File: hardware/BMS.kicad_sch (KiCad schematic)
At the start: 21 parts, among them U3 BQ25887

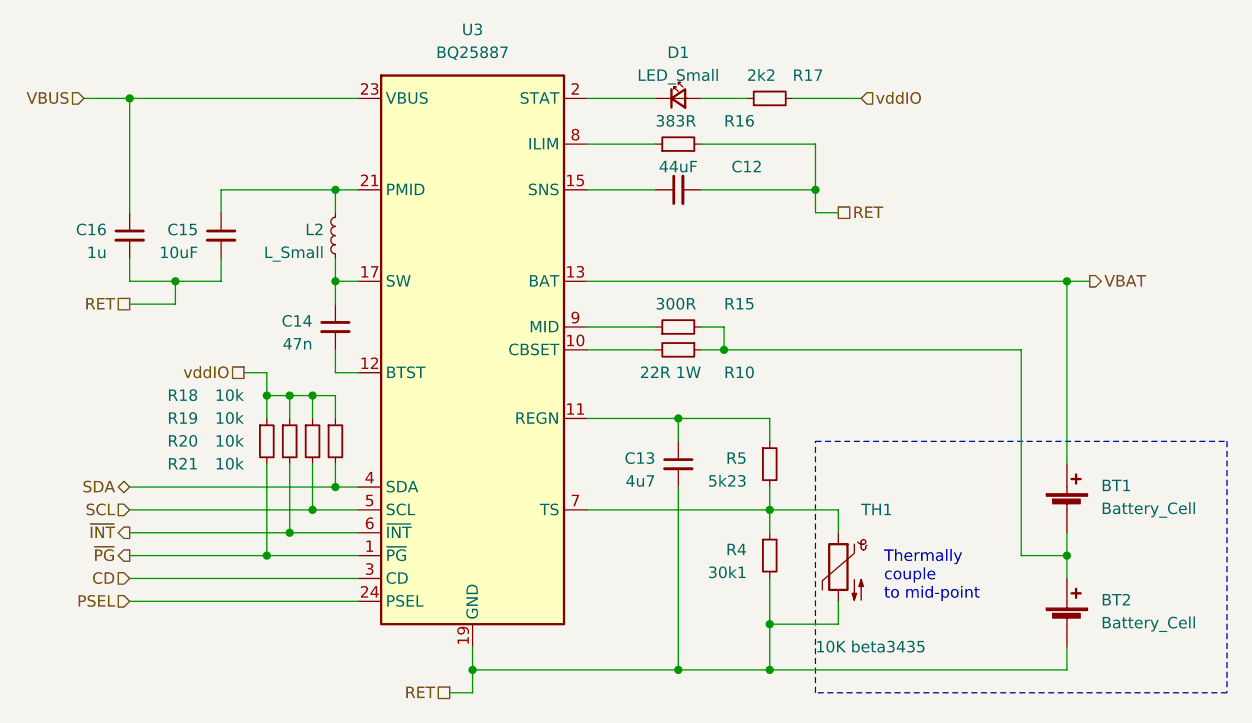
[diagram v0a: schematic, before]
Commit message: Some routing and pinout changes
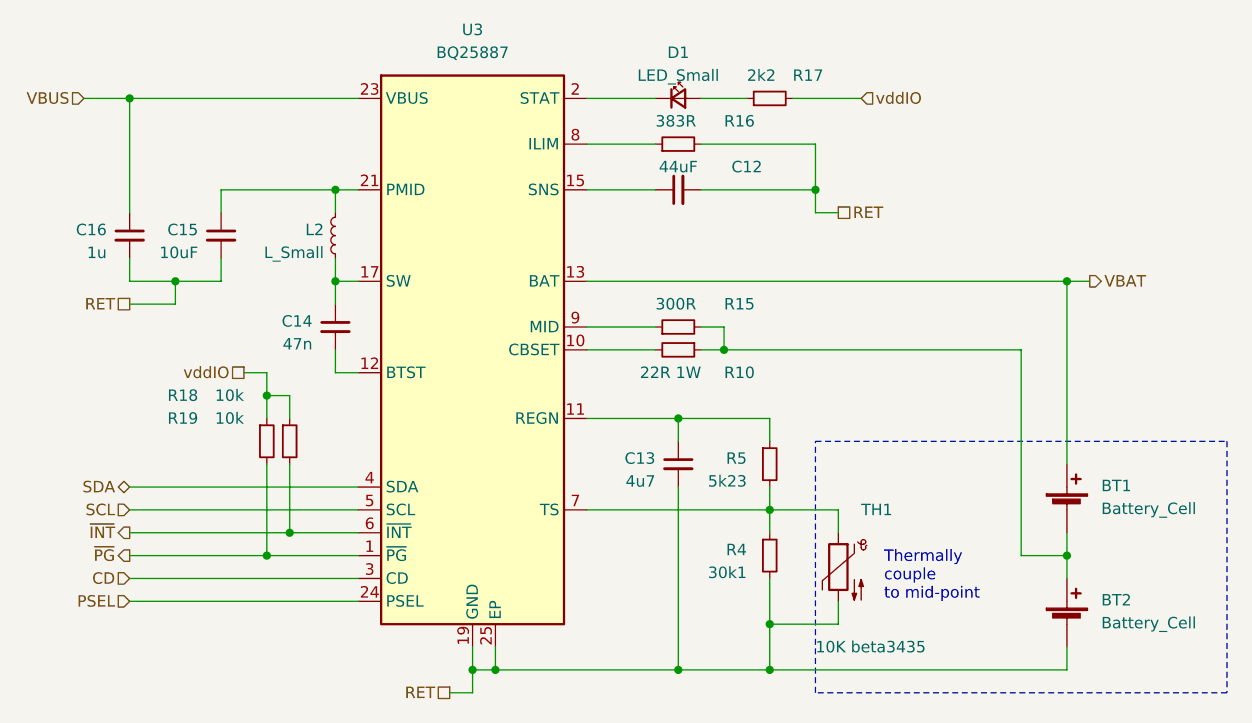
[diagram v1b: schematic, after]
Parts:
- removed R20, R21: 10k, symbol Device:R_Small
- C12: footprint (none) -> Capacitor_SMD:C_1210_3225Metric
- C13: footprint (none) -> Capacitor_SMD:C_0603_1608Metric
- C14, C16: footprint (none) -> Capacitor_SMD:C_0402_1005Metric
- C15: footprint (none) -> Capacitor_SMD:C_0805_2012Metric
- D1: footprint (none) -> LED_SMD:LED_0603_1608Metric
- R10: footprint (none) -> Resistor_SMD:R_1210_3225Metric
- R15: footprint (none) -> Resistor_SMD:R_0603_1608Metric
- R16, R17, R18, R19, R4, R5, TH1: footprint (none) -> Resistor_SMD:R_0402_1005Metric
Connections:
- net RET: now also U3.25 (EP)
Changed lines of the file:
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@@
 (kicad_sch (version 20230121) (generator eeschema)
   (paper "A4")
-  (junction (at 101.6 83.82) (diameter 0) (color 0 0 0 0)
-  )
   (junction (at 96.52 83.82) (diameter 0) (color 0 0 0 0)
   )
@@
   (junction (at 152.4 114.3) (diameter 0) (color 0 0 0 0)
   )
-  (junction (at 101.6 96.52) (diameter 0) (color 0 0 0 0)
-  )
   (junction (at 142.24 86.36) (diameter 0) (color 0 0 0 0)
   )
@@
   (junction (at 147.32 78.74) (diameter 0) (color 0 0 0 0)
   )
-  (junction (at 99.06 83.82) (diameter 0) (color 0 0 0 0)
-  )
   (junction (at 185.42 101.6) (diameter 0) (color 0 0 0 0)
   )
   (junction (at 152.4 96.52) (diameter 0) (color 0 0 0 0)
   )
+  (junction (at 121.92 114.3) (diameter 0) (color 0 0 0 0)
+  )
   (junction (at 104.14 60.96) (diameter 0) (color 0 0 0 0)
   )
@@
   (junction (at 152.4 109.22) (diameter 0) (color 0 0 0 0)
   )
-  (junction (at 104.14 93.98) (diameter 0) (color 0 0 0 0)
-  )
   (junction (at 81.28 50.8) (diameter 0) (color 0 0 0 0)
   )
@@
     (stroke (width 0) (type default))
   )
-  (wire (pts (xy 101.6 91.44) (xy 101.6 96.52))
-    (stroke (width 0) (type default))
-  )
   (wire (pts (xy 154.94 50.8) (xy 162.56 50.8))
     (stroke (width 0) (type default))
   )
-  (wire (pts (xy 119.38 114.3) (xy 142.24 114.3))
+  (wire (pts (xy 119.38 114.3) (xy 121.92 114.3))
     (stroke (width 0) (type default))
   )
@@
     (stroke (width 0) (type default))
   )
-  (wire (pts (xy 101.6 83.82) (xy 104.14 83.82))
-    (stroke (width 0) (type default))
-  )
   (wire (pts (xy 152.4 93.98) (xy 152.4 96.52))
     (stroke (width 0) (type default))
@@
     (stroke (width 0) (type default))
   )
-  (wire (pts (xy 101.6 83.82) (xy 101.6 86.36))
-    (stroke (width 0) (type default))
-  )
-  (wire (pts (xy 99.06 83.82) (xy 101.6 83.82))
-    (stroke (width 0) (type default))
-  )
-  (wire (pts (xy 81.28 93.98) (xy 104.14 93.98))
+  (wire (pts (xy 81.28 93.98) (xy 106.68 93.98))
     (stroke (width 0) (type default))
   )
@@
     (stroke (width 0) (type default))
   )
-  (wire (pts (xy 104.14 83.82) (xy 104.14 86.36))
-    (stroke (width 0) (type default))
-  )
   (wire (pts (xy 132.08 86.36) (xy 142.24 86.36))
     (stroke (width 0) (type default))
@@
     (stroke (width 0) (type default))
   )
-  (wire (pts (xy 104.14 91.44) (xy 104.14 93.98))
-    (stroke (width 0) (type default))
-  )
   (wire (pts (xy 104.14 63.5) (xy 104.14 60.96))
     (stroke (width 0) (type default))
@@
     (stroke (width 0) (type default))
   )
-  (wire (pts (xy 104.14 93.98) (xy 106.68 93.98))
-    (stroke (width 0) (type default))
-  )
   (wire (pts (xy 76.2 50.8) (xy 81.28 50.8))
     (stroke (width 0) (type default))
@@
     (stroke (width 0) (type default))
   )
+  (wire (pts (xy 121.92 111.76) (xy 121.92 114.3))
+    (stroke (width 0) (type default))
+  )
   (wire (pts (xy 93.98 81.28) (xy 96.52 81.28))
     (stroke (width 0) (type default))
@@
     (stroke (width 0) (type default))
   )
-  (wire (pts (xy 81.28 96.52) (xy 101.6 96.52))
-    (stroke (width 0) (type default))
-  )
   (wire (pts (xy 81.28 50.8) (xy 106.68 50.8))
     (stroke (width 0) (type default))
@@
     (stroke (width 0) (type default))
   )
-  (wire (pts (xy 101.6 96.52) (xy 106.68 96.52))
+  (wire (pts (xy 121.92 114.3) (xy 142.24 114.3))
+    (stroke (width 0) (type default))
+  )
+  (wire (pts (xy 81.28 96.52) (xy 106.68 96.52))
     (stroke (width 0) (type default))
   )
@@
       (effects (font (size 1.27 1.27)) (justify right))
     )
-    (property "Footprint" "" (at 96.52 88.9 0)
+    (property "Footprint" "Resistor_SMD:R_0402_1005Metric" (at 96.52 88.9 0)
       (effects (font (size 1.27 1.27)) hide)
     )
@@
       (effects (font (size 1.27 1.27)) (justify right))
     )
-    (property "Footprint" "" (at 152.4 50.8 0)
+    (property "Footprint" "Resistor_SMD:R_0402_1005Metric" (at 152.4 50.8 0)
       (effects (font (size 1.27 1.27)) hide)
     )
@@
       (effects (font (size 1.27 1.27)) (justify right))
     )
-    (property "Footprint" "" (at 142.24 91.44 0)
+    (property "Footprint" "Capacitor_SMD:C_0603_1608Metric" (at 142.24 91.44 0)
       (effects (font (size 1.27 1.27)) hide)
     )
@@
       (effects (font (size 1.27 1.27)) (justify right))
     )
-    (property "Footprint" "" (at 104.14 76.2 0)
+    (property "Footprint" "Capacitor_SMD:C_0402_1005Metric" (at 104.14 76.2 0)
       (effects (font (size 1.27 1.27)) hide)
     )
@@
       (effects (font (size 1.27 1.27)))
     )
-    (property "Footprint" "" (at 142.24 60.96 0)
+    (property "Footprint" "Capacitor_SMD:C_1210_3225Metric" (at 142.24 60.96 0)
       (effects (font (size 1.27 1.27)) hide)
     )
@@
       (effects (font (size 1.27 1.27)) (justify right))
     )
-    (property "Footprint" "" (at 160.02 101.6 0)
+    (property "Footprint" "Resistor_SMD:R_0402_1005Metric" (at 160.02 101.6 0)
       (effects (font (size 1.27 1.27)) hide)
     )
@@
       (effects (font (size 1.27 1.27)) (justify right))
     )
-    (property "Footprint" "" (at 142.24 76.2 0)
+    (property "Footprint" "Resistor_SMD:R_0603_1608Metric" (at 142.24 76.2 0)
       (effects (font (size 1.27 1.27)) hide)
     )
@@
       (effects (font (size 1.27 1.27)))
     )
-    (property "Footprint" "" (at 142.24 50.8 90)
+    (property "Footprint" "LED_SMD:LED_0603_1608Metric" (at 142.24 50.8 90)
       (effects (font (size 1.27 1.27)) hide)
     )
@@
       (effects (font (size 1.27 1.27)) (justify right))
     )
-    (property "Footprint" "" (at 81.28 66.04 0)
+    (property "Footprint" "Capacitor_SMD:C_0402_1005Metric" (at 81.28 66.04 0)
       (effects (font (size 1.27 1.27)) hide)
     )
@@
       (effects (font (size 1.27 1.27)) (justify right))
     )
-    (property "Footprint" "" (at 142.24 55.88 0)
+    (property "Footprint" "Resistor_SMD:R_0402_1005Metric" (at 142.24 55.88 0)
       (effects (font (size 1.27 1.27)) hide)
     )
@@
       (effects (font (size 1.27 1.27)) (justify right))
     )
-    (property "Footprint" "" (at 152.4 101.6 0)
+    (property "Footprint" "Resistor_SMD:R_0402_1005Metric" (at 152.4 101.6 0)
       (effects (font (size 1.27 1.27)) hide)
     )
@@
     )
   )
-  (symbol (lib_id "Device:R_Small") (at 101.6 88.9 0) (unit 1)
-    (in_bom yes) (on_board yes) (dnp no)
-    (property "Reference" "R20" (at 88.9 88.9 0)
-      (effects (font (size 1.27 1.27)) (justify right))
-    )
-    (property "Value" "10k" (at 93.98 88.9 0)
-      (effects (font (size 1.27 1.27)) (justify right))
-    )
-    (property "Footprint" "" (at 101.6 88.9 0)
-      (effects (font (size 1.27 1.27)) hide)
-    )
-    (property "Datasheet" "~" (at 101.6 88.9 0)
-      (effects (font (size 1.27 1.27)) hide)
-    )
-    (pin "1")
-    (pin "2")
-    (instances
-      (project "USB-PD_lipo"
-        (path "/0ce26e5f-6628-4058-9647-c7a8354a5e67/75d9acb4-46f2-4f45-b740-fe8577c2e31d"
-          (reference "R20") (unit 1)
-        )
-      )
-    )
-  )
   (symbol (lib_id "Device:R_Small") (at 152.4 91.44 0) (unit 1)
     (in_bom yes) (on_board yes) (dnp no)
@@
       (effects (font (size 1.27 1.27)) (justify right))
     )
-    (property "Footprint" "" (at 152.4 91.44 0)
+    (property "Footprint" "Resistor_SMD:R_0402_1005Metric" (at 152.4 91.44 0)
       (effects (font (size 1.27 1.27)) hide)
     )
@@
       (effects (font (size 1.27 1.27)) (justify right))
     )
-    (property "Footprint" "" (at 142.24 78.74 0)
+    (property "Footprint" "Resistor_SMD:R_1210_3225Metric" (at 142.24 78.74 0)
       (effects (font (size 1.27 1.27)) hide)
     )
@@
       (effects (font (size 1.27 1.27)) (justify right))
     )
-    (property "Footprint" "" (at 91.44 66.04 0)
+    (property "Footprint" "Capacitor_SMD:C_0805_2012Metric" (at 91.44 66.04 0)
       (effects (font (size 1.27 1.27)) hide)
     )
@@
     (pin "23")
     (pin "24")
+    (pin "25")
     (pin "3")
     (pin "4")
@@
       (effects (font (size 1.27 1.27)) (justify right))
     )
-    (property "Footprint" "" (at 99.06 88.9 0)
+    (property "Footprint" "Resistor_SMD:R_0402_1005Metric" (at 99.06 88.9 0)
       (effects (font (size 1.27 1.27)) hide)
     )
@@
         )
       )
-    )
-  )
-  (symbol (lib_id "Device:R_Small") (at 104.14 88.9 0) (unit 1)
-    (in_bom yes) (on_board yes) (dnp no)
-    (property "Reference" "R21" (at 88.9 91.44 0)
-      (effects (font (size 1.27 1.27)) (justify right))
-    )
-    (property "Value" "10k" (at 93.98 91.44 0)
-      (effects (font (size 1.27 1.27)) (justify right))
-    )
-    (property "Footprint" "" (at 104.14 88.9 0)
-      (effects (font (size 1.27 1.27)) hide)
-    )
-    (property "Datasheet" "~" (at 104.14 88.9 0)
-      (effects (font (size 1.27 1.27)) hide)
-    )
-    (pin "1")
-    (pin "2")
-    (instances
-      (project "USB-PD_lipo"
-        (path "/0ce26e5f-6628-4058-9647-c7a8354a5e67/75d9acb4-46f2-4f45-b740-fe8577c2e31d"
-          (reference "R21") (unit 1)
-        )
-      )
